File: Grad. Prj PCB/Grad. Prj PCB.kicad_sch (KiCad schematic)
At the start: 45 parts, among them J1 GPS, J2 Lock_4, J3 Lock_3, J4 Lock_2, J5 Lock_1, J6 POWER INPUT, J7 Pressure, J8 Heart Rate, J9 Vbatt, K1 POWER RELAY, Q1 BC337, Q2 BC337, Q3 BC337, Q4 BC337, Q5 BC337, U1 ATmega128-16A, U2 SIM800L-CORE, U3 YAAJ_DCDC_StepDown_LM2596, U4 L7805, U5 DS1307+, Y1 Crystal, Y2 Crystal

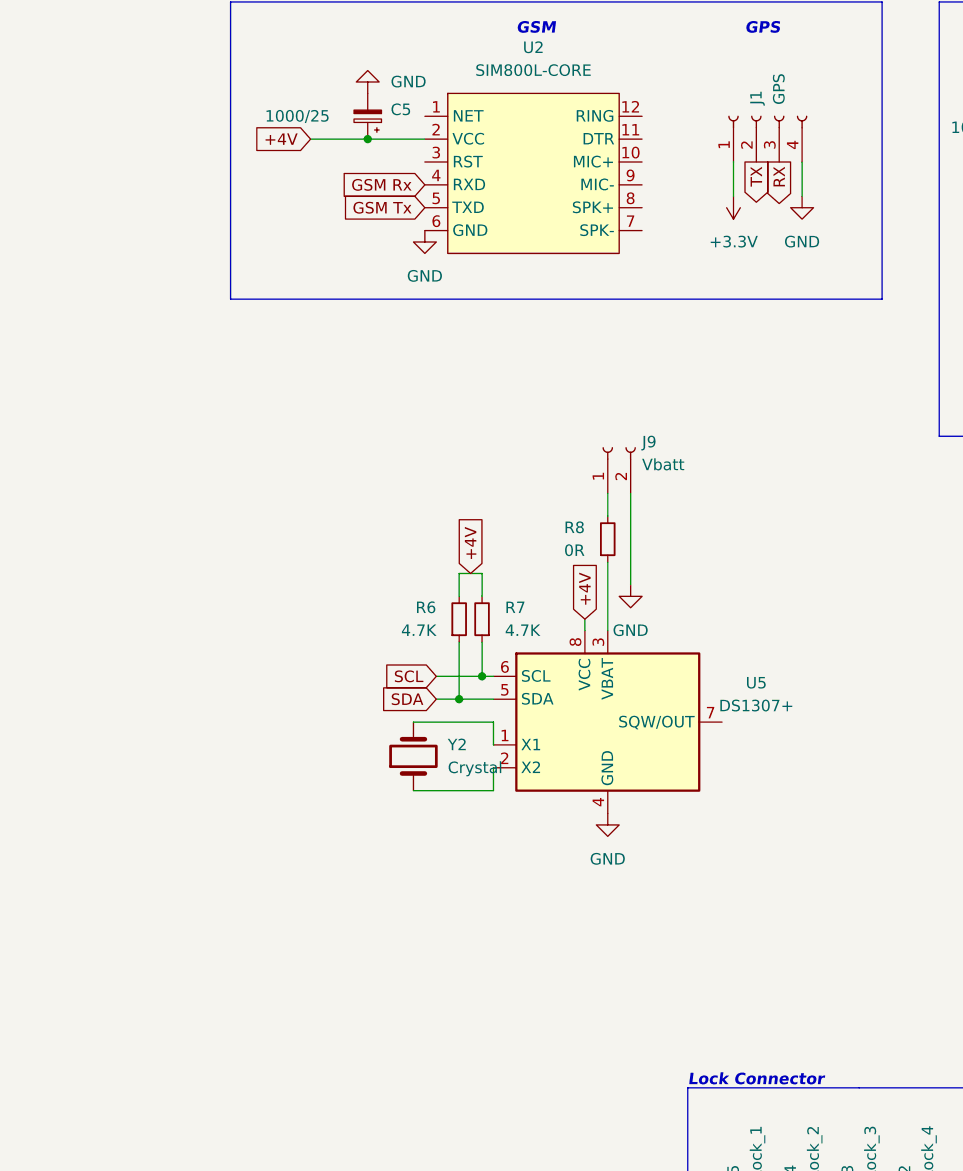
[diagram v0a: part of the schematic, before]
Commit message: Added RTC
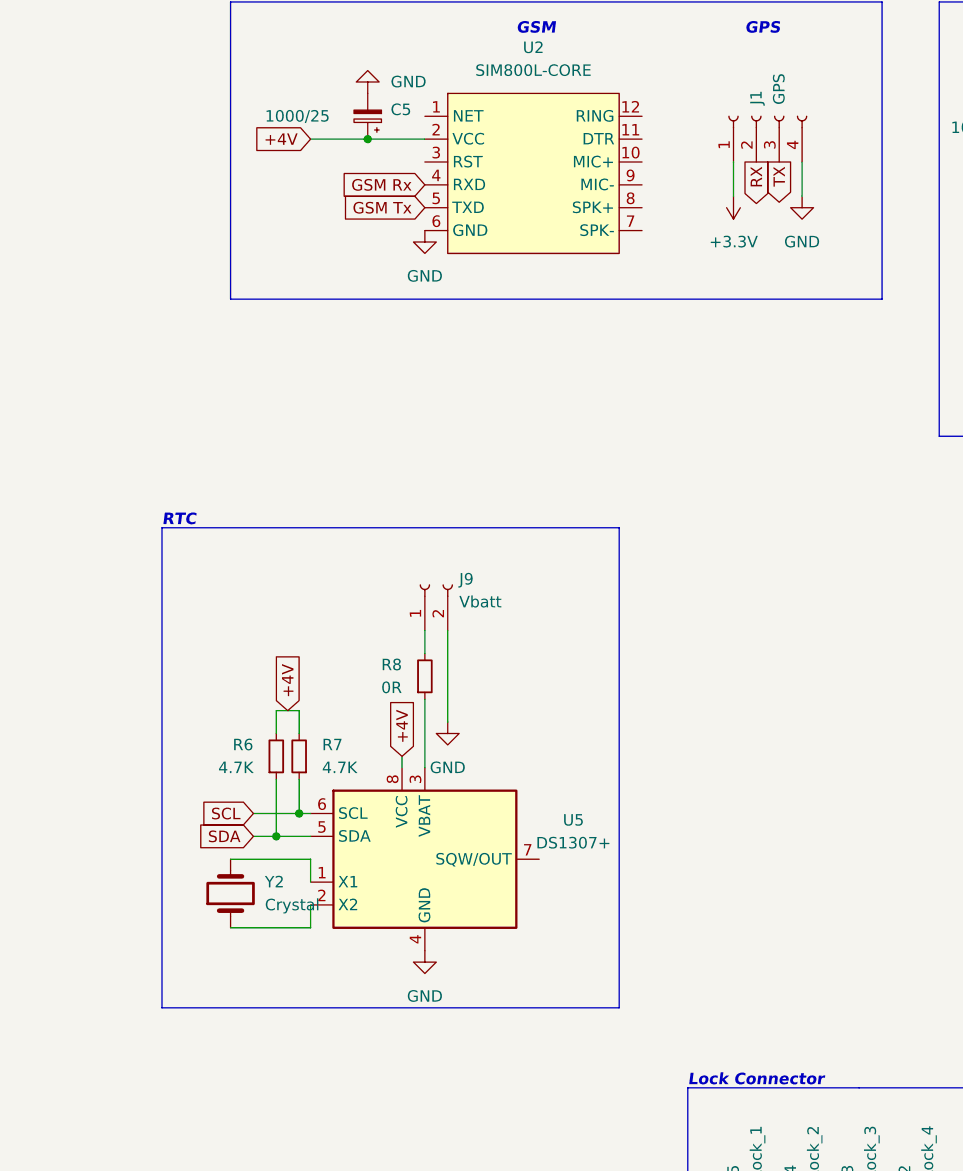
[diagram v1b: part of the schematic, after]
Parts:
- J1: footprint (none) -> Connector_PinHeader_2.54mm:PinHeader_1x04_P2.54mm_Vertical
- J8: footprint (none) -> Connector_PinSocket_2.54mm:PinSocket_1x03_P2.54mm_Vertical
- U4: footprint (none) -> Package_TO_SOT_THT:TO-220-3_Vertical
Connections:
- net RX: now also J1.2 (Pin_2); no longer J1.3 (Pin_3)
- net TX: now also J1.3 (Pin_3); no longer J1.2 (Pin_2)
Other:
- note added: "RTC"
- moved on the sheet: J9, R6, R7, R8, U5, Y2

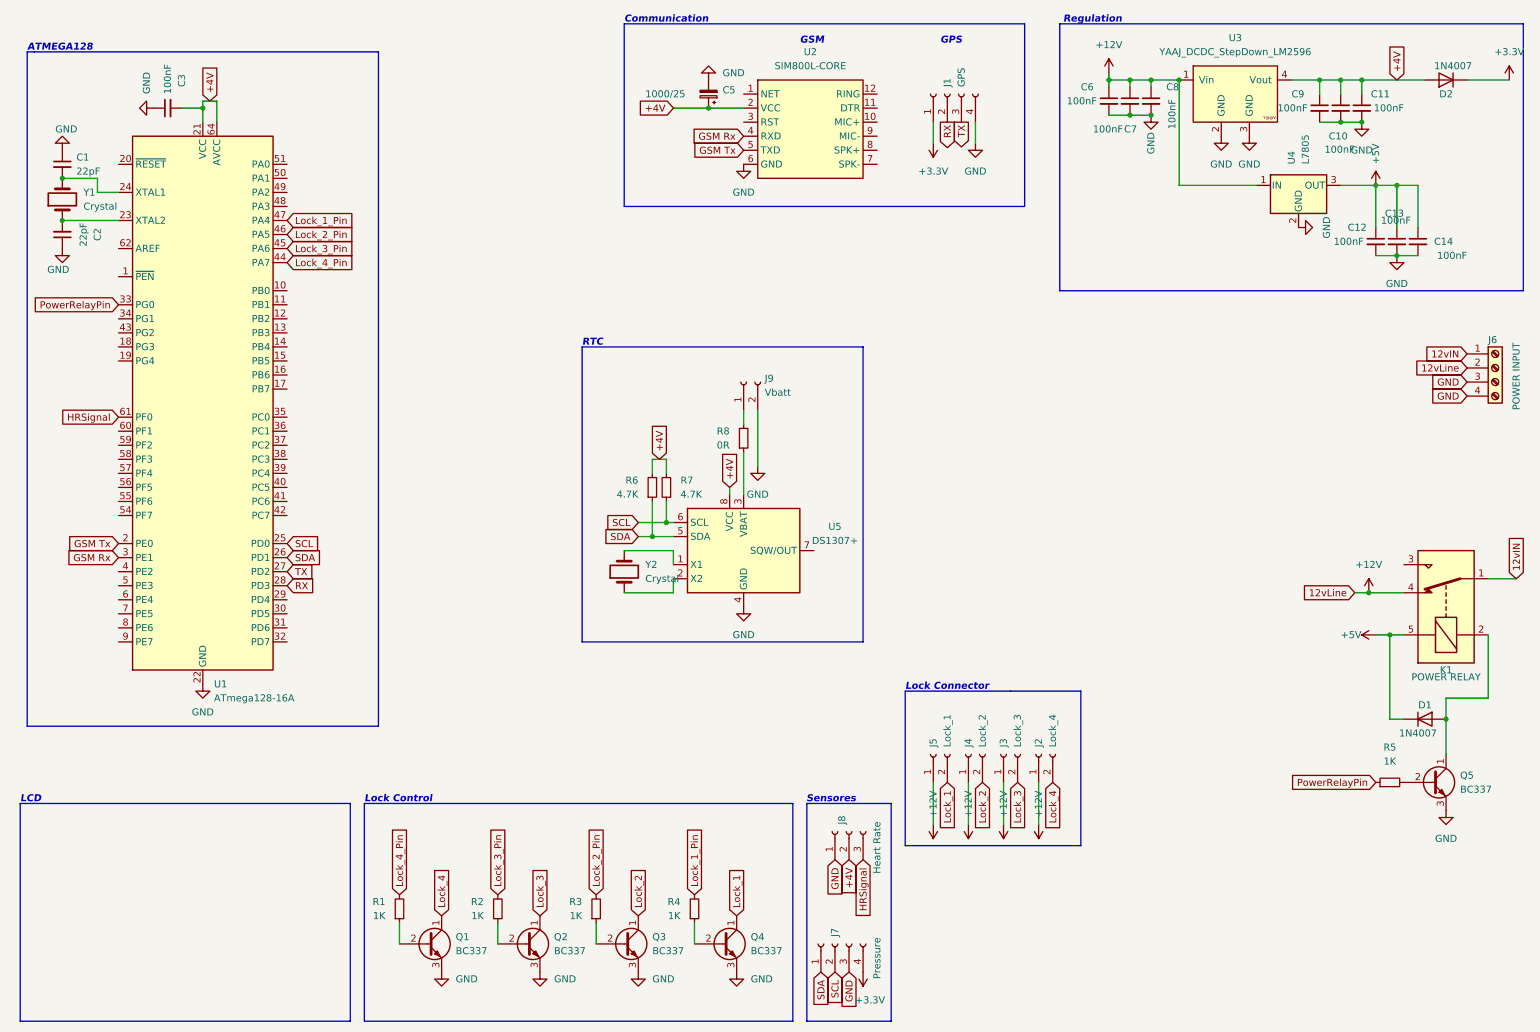
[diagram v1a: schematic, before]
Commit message: Added ISP Header
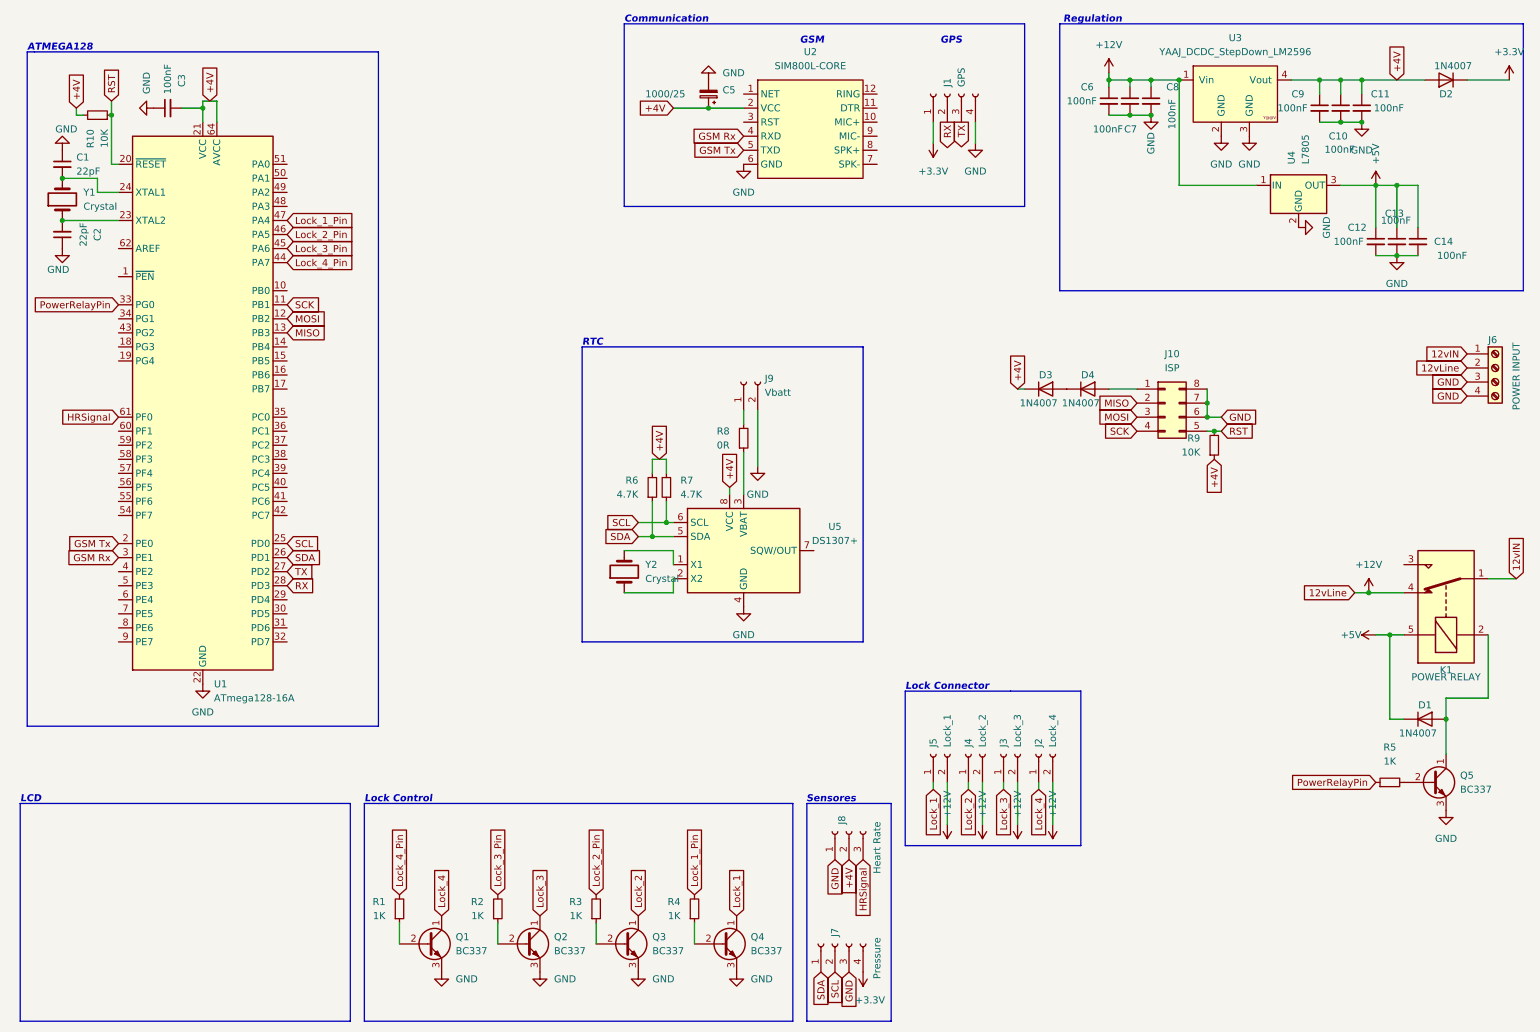
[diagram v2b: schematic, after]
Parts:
- added D3, D4: 1N4007, Diode_THT:D_DO-41_SOD81_P10.16mm_Horizontal, symbol Diode:1N4007
- added J10: ISP, symbol Connector_Generic:Conn_02x04_Counter_Clockwise
- added R10, R9: 10K, Resistor_THT:R_Axial_DIN0207_L6.3mm_D2.5mm_P7.62mm_Horizontal, symbol Device:R_Small
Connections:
- net +12V: now also J2.2 (Pin_2), J3.2 (Pin_2), J4.2 (Pin_2), J5.2 (Pin_2); no longer J2.1 (Pin_1), J3.1 (Pin_1), J4.1 (Pin_1), J5.1 (Pin_1)
- net +4V: now also D3.1 (K), R10.2, R9.1
- net GND: now also J10.6 (Pin_6), J10.7 (Pin_7), J10.8 (Pin_8)
- net Lock_1: now also J5.1 (Pin_1); no longer J5.2 (Pin_2)
- net Lock_2: now also J4.1 (Pin_1); no longer J4.2 (Pin_2)
- net Lock_3: now also J3.1 (Pin_1); no longer J3.2 (Pin_2)
- net Lock_4: now also J2.1 (Pin_1); no longer J2.2 (Pin_2)
- net SCK: now reaches U1.11 (PB1)
- net SCK: now also J10.4 (Pin_4)
- net MOSI: now reaches U1.12 (PB2)
- net MOSI: now also J10.3 (Pin_3)
- net MISO: now reaches U1.13 (PB3)
- net MISO: now also J10.2 (Pin_2)
- net RST: now reaches U1.20 (~{RESET})
- net RST: now also J10.5 (Pin_5), R10.1, R9.2
- new net: D4.2 (A), J10.1 (Pin_1)
- new net: D3.2 (A), D4.1 (K)

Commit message: Add Lpf and Acc Line in Sch and Brd
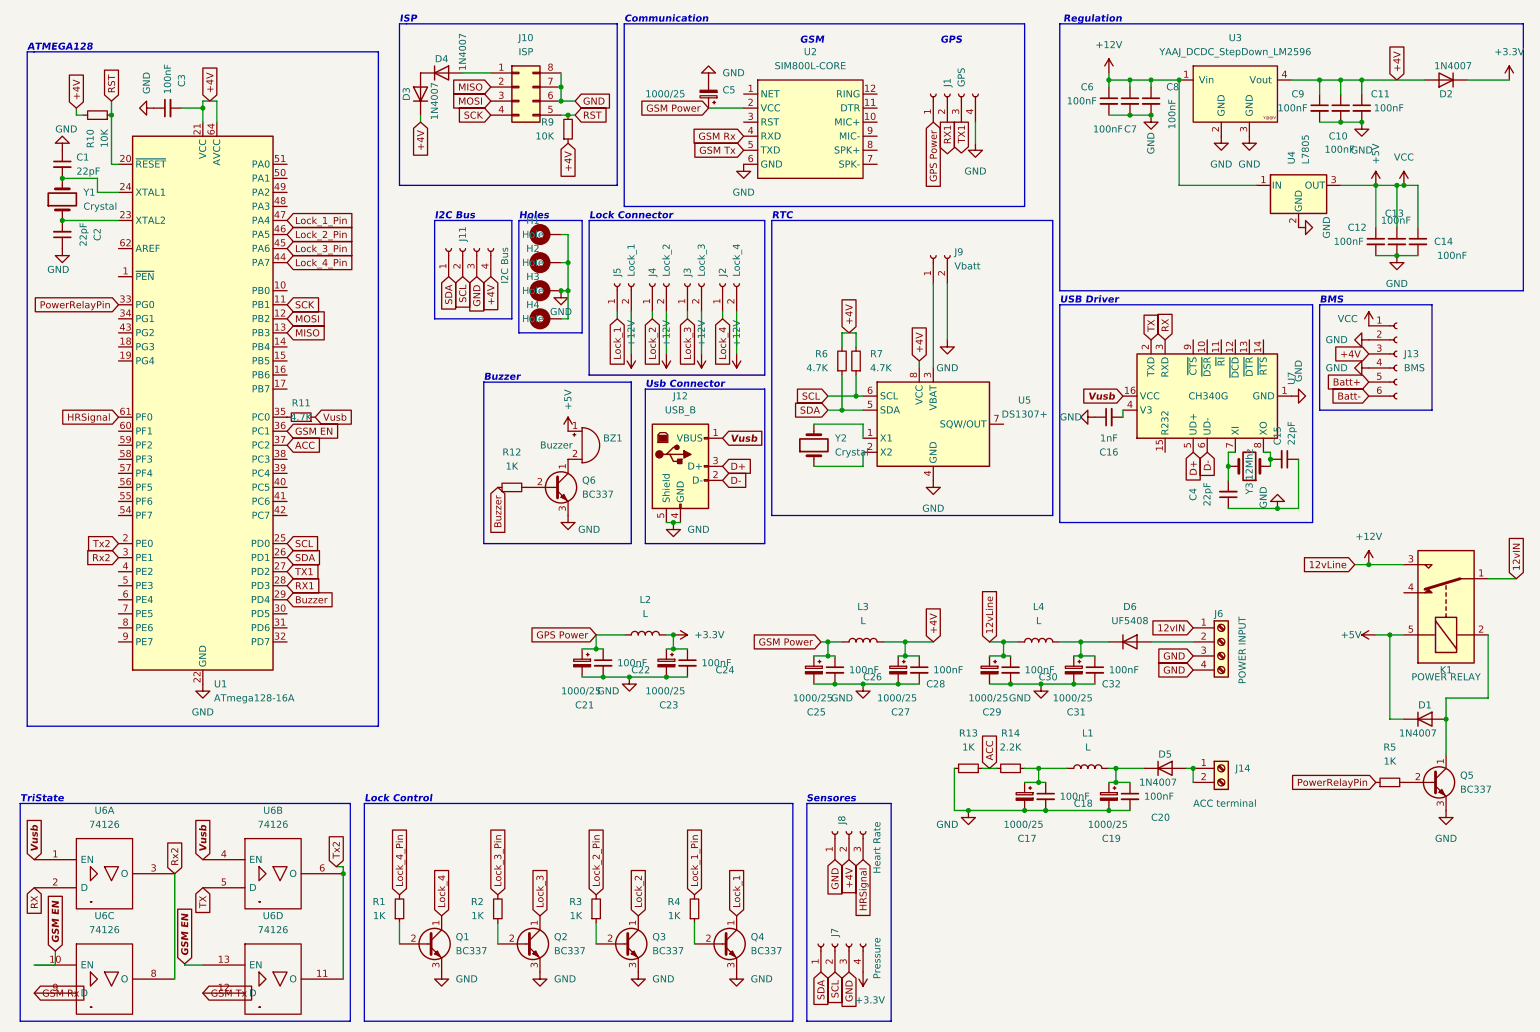
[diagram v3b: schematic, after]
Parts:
- removed R8: 0R, Resistor_THT:R_Axial_DIN0207_L6.3mm_D2.5mm_P7.62mm_Horizontal, symbol Device:R_Small
- added BZ1: Buzzer, Buzzer_Beeper:Buzzer_12x9.5RM7.6, symbol Device:Buzzer
- added C15, C4: 22pF, Capacitor_THT:C_Disc_D3.8mm_W2.6mm_P2.50mm, symbol Device:C_Small
- added C16: 1nF, Capacitor_THT:C_Disc_D3.8mm_W2.6mm_P2.50mm, symbol Device:C_Small
- added C17, C19, C21, C23, C25, C27, C29, C31: 1000/25, Capacitor_THT:CP_Radial_D8.0mm_P3.80mm, symbol Device:C_Polarized_Small
- added C18, C20, C22, C24, C26, C28, C30, C32: 100nF, Capacitor_THT:C_Disc_D4.3mm_W1.9mm_P5.00mm, symbol Device:C_Small
- added D5: 1N4007, Diode_THT:D_DO-41_SOD81_P10.16mm_Horizontal, symbol Diode:1N4007
- added D6: UF5408, Diode_THT:D_DO-201AD_P15.24mm_Horizontal, symbol Diode:UF5408
- added H1, H2, H3: Hole, MountingHole:MountingHole_3.2mm_M3_ISO7380_Pad, symbol Mechanical:MountingHole_Pad
- added H4: Hole, symbol Mechanical:MountingHole_Pad
- added J11: I2C Bus, Connector_PinHeader_2.54mm:PinHeader_1x04_P2.54mm_Vertical, symbol Connector:Conn_01x04_Female
- added J12: USB_B, Connector_USB:USB_B_OST_USB-B1HSxx_Horizontal, symbol Connector:USB_B
- added J13: BMS, BMS:TP4056-Module, symbol Connector:Conn_01x06_Female
- added J14: ACC terminal, symbol Connector:Screw_Terminal_01x02
- added L1, L4: L, symbol Device:L
- added L2: L, Inductor_THT:L_Axial_L6.6mm_D2.7mm_P10.16mm_Horizontal_Vishay_IM-2, symbol Device:L
- added L3: L, Inductor_SMD:L_6.3x6.3_H3, symbol Device:L
- added Q6: BC337, Package_TO_SOT_THT:TO-92_Inline, symbol Transistor_BJT:BC337
- added R11: 4.7K, Resistor_THT:R_Axial_DIN0207_L6.3mm_D2.5mm_P7.62mm_Horizontal, symbol Device:R_Small
- added R12, R13: 1K, Resistor_THT:R_Axial_DIN0207_L6.3mm_D2.5mm_P7.62mm_Horizontal, symbol Device:R_Small
- added R14: 2.2K, Resistor_THT:R_Axial_DIN0207_L6.3mm_D2.5mm_P7.62mm_Horizontal, symbol Device:R_Small
- added U6: 74126, Package_DIP:DIP-14_W7.62mm_LongPads, symbol 74xx_IEEE:74126
- added U7: CH340G, Package_SO:SOIC-16_3.9x9.9mm_P1.27mm, symbol Interface_USB:CH340G
- added Y3: 12Mhz, Crystal:Crystal_HC49-4H_Vertical, symbol Device:Crystal
- J10: footprint (none) -> Connector_PinSocket_2.54mm:PinSocket_2x04_P2.54mm_Vertical
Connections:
- net +12V: now also K1.3, C29.1, C30.1, L4.1; no longer J6.2 (Pin_2), K1.4
- net +3.3V: now also C23.1, C24.1, L2.2; no longer J1.1 (Pin_1)
- net +4V: now also C27.1, C28.1, J11.4 (Pin_4), J13.3 (Pin_3), L3.2; no longer C5.1, U2.2 (VCC)
- net +5V: now also BZ1.1 (-), J13.1 (Pin_1), U6.14 (VCC), U6.14 (VCC), U6.14 (VCC), U6.14 (VCC)
- net GND: now also C15.1, C16.1, C17.2, C18.2, C19.2, C20.2, C21.2, C22.2, C23.2, C24.2, C25.2, C26.2, C27.2, C28.2, C29.2, C30.2, C31.2, C32.2, C4.1, H1.1, H2.1, H3.1, H4.1, J11.3 (Pin_3), J12.4 (GND), J12.5 (Shield), J13.2 (Pin_2), J13.4 (Pin_4), Q6.3 (E), R13.2, U6.7 (GND), U6.7 (GND), U6.7 (GND), U6.7 (GND), U7.1 (GND)
- net GSM Rx: now also U6.9 (D); no longer U1.3 (PE1)
- net GSM Tx: now also U6.12 (D); no longer U1.2 (PE0)
- net RX: now also U6.2 (D), U7.3 (RXD); no longer J1.2 (Pin_2), U1.28 (PD3)
- net SCL: now also J11.2 (Pin_2)
- net SDA: now also J11.1 (Pin_1)
- net TX: now also U6.5 (D), U7.2 (TXD); no longer J1.3 (Pin_3), U1.27 (PD2)
- net at U5.3 (VBAT): now also J9.1 (Pin_1)
- net Buzzer: now reaches U1.29 (PD4)
- net Buzzer: now also R12.1
- net at U1.35 (PC0): now also R11.2
- net GSM EN: now reaches U1.36 (PC1)
- net GSM EN: now also U6.10 (EN), U6.13 (EN)
- net ACC: now reaches U1.37 (PC2)
- net ACC: now also R13.1, R14.2
- new net: C19.1, C20.1, D5.1 (K), L1.2
- new net: BZ1.2 (+), Q6.1 (C)
- new net: C15.2, U7.8 (XO), Y3.1
- new net: C4.2, U7.7 (XI), Y3.2
- new net: C17.1, C18.1, L1.1, R14.1
- new net: Q6.2 (B), R12.2
- new net: D5.2 (A), J14.1 (Pin_1), J14.2 (Pin_2)
- new net: C31.1, C32.1, D6.1 (K), L4.2
- new net: D6.2 (A), J6.2 (Pin_2)
- new net: C16.2, U7.4 (V3)
- new net Batt+: J13.5 (Pin_5)
- new net Batt-: J13.6 (Pin_6)
- new net D+: J12.3 (D+), U7.5 (UD+)
- new net D-: J12.2 (D-), U7.6 (UD-)
- new net GPS Power: C21.1, C22.1, J1.1 (Pin_1), L2.1
- new net GSM Power: C25.1, C26.1, C5.1, L3.1, U2.2 (VCC)
- new net RX1: J1.2 (Pin_2), U1.28 (PD3)
- new net Rx2: U1.3 (PE1), U6.3 (O), U6.8 (O)
- new net TX1: J1.3 (Pin_3), U1.27 (PD2)
- new net Tx2: U1.2 (PE0), U6.11 (O), U6.6 (O)
- new net Vusb: J12.1 (VBUS), R11.1, U6.1 (EN), U6.4 (EN), U7.16 (VCC)
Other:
- note added: "BMS"
- note added: "Buzzer"
- note added: "Holes"
- note added: "I2C Bus"
- note added: "ISP"
- note added: "TriState"
- note added: "USB Driver"
- note added: "Usb Connector"
- note removed: "LCD"
- moved on the sheet: D3, D4, J10, J2, J3, J4, J5, J6, J9, R6, R7, R9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
